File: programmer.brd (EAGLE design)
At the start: 22.9 x 12.1 mm, 17 parts, among them IC1 MIC5225-3.3v, Q1 BSS138, Q2 BSS138, Q3 BSS138, Q4 BSS138

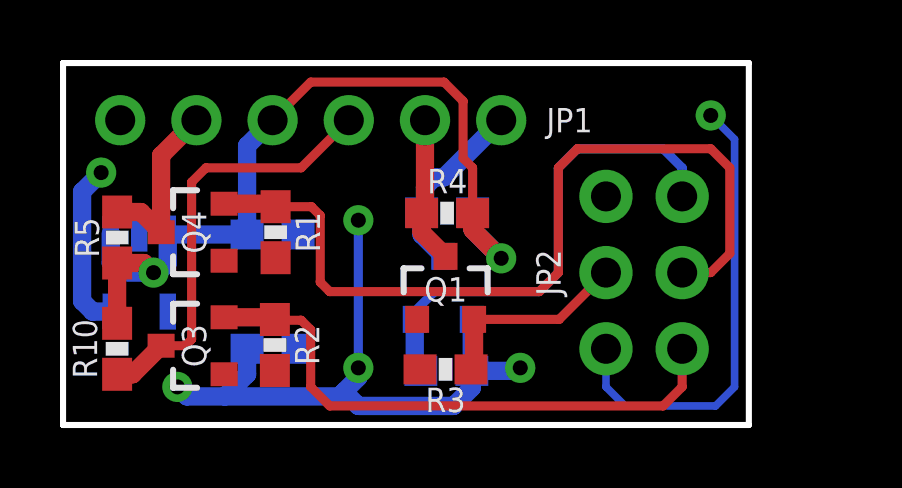
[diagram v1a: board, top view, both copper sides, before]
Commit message: Update ATtiny programming interface board
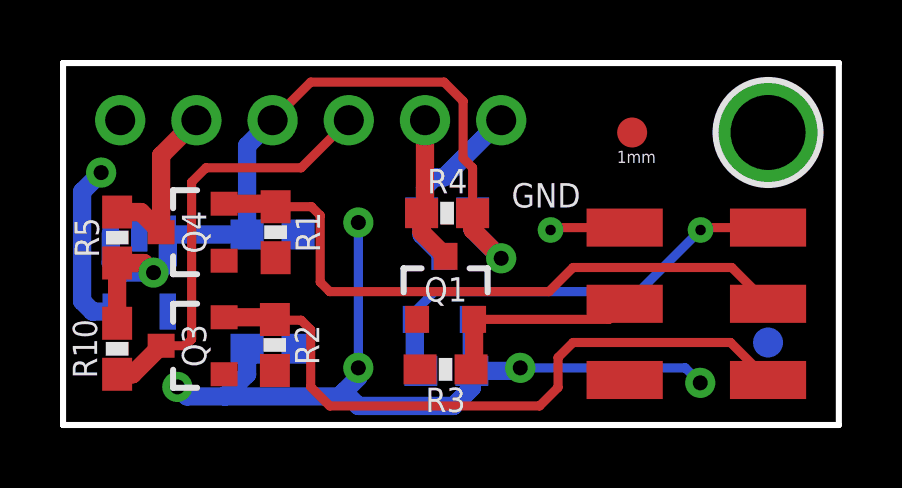
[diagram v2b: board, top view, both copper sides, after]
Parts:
- removed JP2: (no value), microbuilder:2X03_ROUND_70MIL
- added FID1, FID2: FIDUCIAL1X2.5, microbuilder:FIDUCIAL-1X2.5
- added PAD1, PAD2, PAD3, PAD4, PAD5, PAD6: WIREPADSMD1,27-254, wirepad:SMD1,27-2,54
- added U$1: MOUNTINGHOLE2.5, microbuilder:MOUNTINGHOLE_2.5_PLATED
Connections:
- net +3V3: now also PAD1.1; no longer JP2.1
- net CLK_3V3: now also PAD4.1; no longer JP2.4
- net GND: now also PAD5.1; no longer JP2.5
- net MISO_3V3: now also PAD2.1; no longer JP2.2
- net MOSI_3V3: now also PAD3.1; no longer JP2.3
- net RST_3V3: now also PAD6.1; no longer JP2.6
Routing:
- net +3V3: track 43.5 -> 34.2 mm
- net CLK_3V3: track 28.9 -> 22.1 mm
- net MISO_3V3: track 19.2 -> 22.6 mm
- net GND: track 0.00 -> 2.50 mm, vias 0 -> 1
- net RST_3V3: track 16.5 -> 15.0 mm, vias 0 -> 1
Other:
- board size 22.9 x 12.1 mm -> 25.9 x 12.1 mm
- board text added: "GND"
- board text added: "rev. A"
